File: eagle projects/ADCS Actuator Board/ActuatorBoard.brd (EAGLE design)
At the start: 91 x 91 mm, 230 parts, among them J11 TE_1-84953-1, J2 TE_1-84953-1, J4 TE_1-84953-1, U10 LM2917MX/NOPB, U11 BD6210F-E2, U12 TSV991AILT, U13 LM2917MX/NOPB, U14 ADS7841E_2K5, U16 DRV10970_MOTOR_DRIVERDRV10970, U17 LM2917MX/NOPB, U18 BD6210F-E2, U19 TSV991AILT, U20 ADS7841E_2K5, U5 BD6210F-E2, U6 DRV10970_MOTOR_DRIVERDRV10970, U7 DRV10970_MOTOR_DRIVERDRV10970, U8 TSV991AILT, U9 ADS7841E_2K5

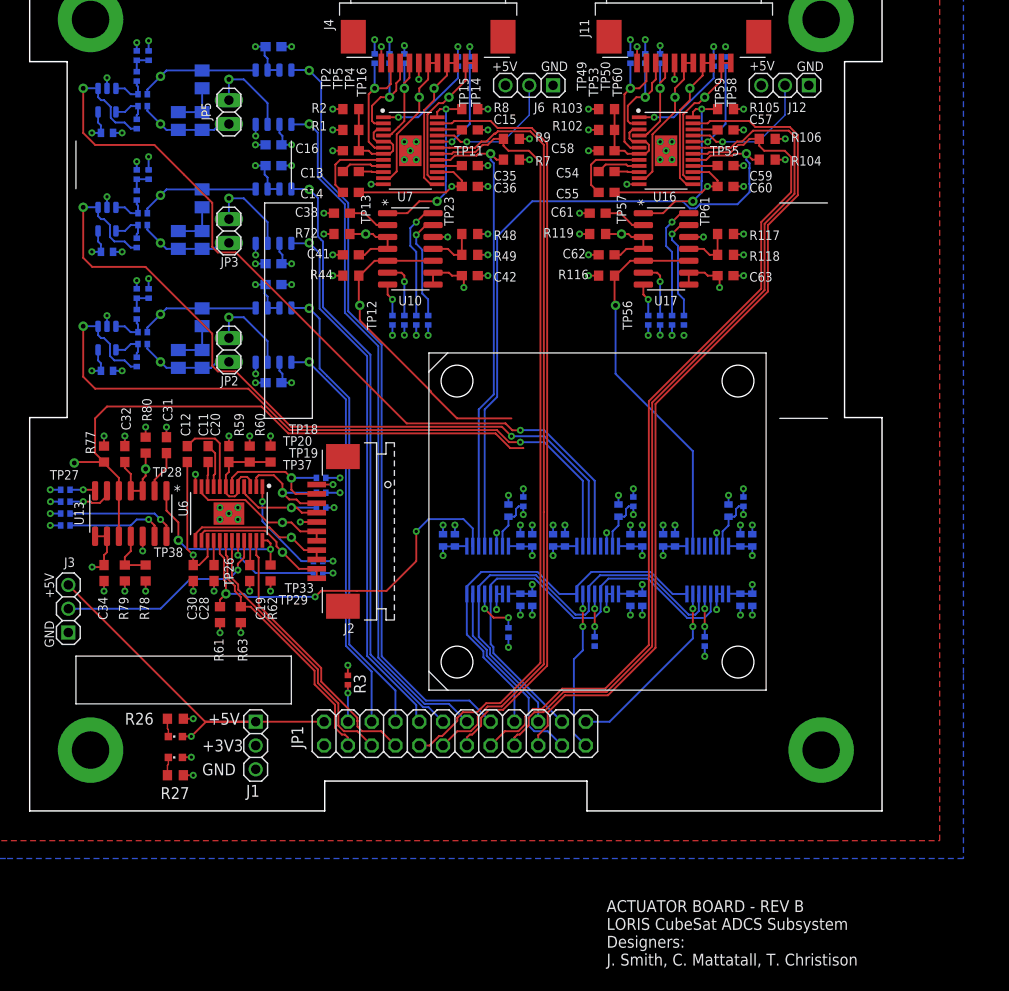
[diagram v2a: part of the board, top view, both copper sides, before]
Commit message: Added power connector and mobo-act brd mounting holes
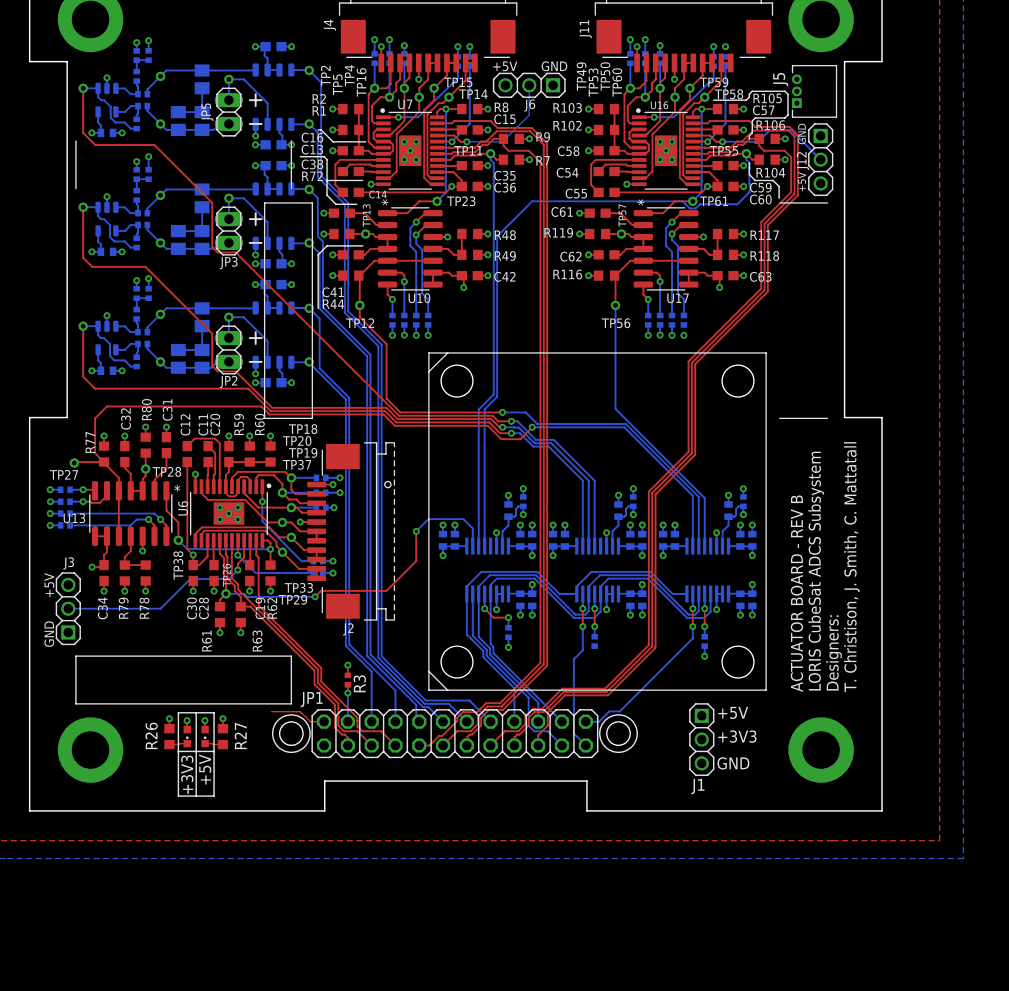
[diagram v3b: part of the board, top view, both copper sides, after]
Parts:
- added J5: TE-1734829-3, my_library:TE-1734829-3
- moved J1 47.6 mm to (71.8, 7.62)
- moved J12 8.80 mm to (84.5, 69.5), turned to 270 degrees
- moved R27 6.55 mm to (20.6, 7.94), turned to 270 degrees
- moved LED2 3.88 mm to (18.7, 7.94), turned to 180 degrees
- moved R26 2.01 mm to (14.9, 7.94), turned to 270 degrees
- moved LED1 1.27 mm to (16.8, 7.94), turned to 180 degrees
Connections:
- net +3V3: now also J5.2
- net +5V: now also J5.1
- net GND: now also J5.3
- net RW_Y_SPD: now also U20.4; no longer U20.2
- net RW_Z_SPD: now also U20.2; no longer U20.4
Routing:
- net +5V: track 146.0 -> 111.2 mm
- net RW_X_SPD: track 34.0 -> 65.9 mm, vias 0 -> 1
- net RW_Z_SPD: track 64.9 -> 91.6 mm, vias 0 -> 1
- net BRKMOD_Y: track 14.5 -> 15.8 mm
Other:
- board text added: "T. Christison, J. Smith, C. Mattatall"
- board text added: "TOP SIDE VIAS COVERED WITH SOLDERMASK"
- board text removed: "J. Smith, C. Mattatall, T. Christison"

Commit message: Rev B almost ready
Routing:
- net N$2: track 6.72 -> 0.00 mm, vias 1 -> 0
- net N$7: track 6.72 -> 0.00 mm, vias 1 -> 0
- net N$4: track 6.72 -> 0.00 mm, vias 1 -> 0
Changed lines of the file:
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@@
 <wire x1="24.13" y1="76.5175" x2="24.13" y2="75.2475" width="0.2032" layer="25"/>
 <wire x1="23.495" y1="73.3425" x2="24.765" y2="73.3425" width="0.2032" layer="25"/>
-<text x="0.635" y="96.52" size="1.778" layer="48">TOP SIDE VIAS COVERED WITH SOLDERMASK</text>
+<text x="0" y="93.345" size="1.778" layer="48">TOP SIDE VIAS COVERED WITH SOLDERMASK</text>
 <hole x="62.865" y="8.255" drill="2.5"/>
 <hole x="27.94" y="8.255" drill="2.5"/>
@@
 <wire x1="18.415" y1="74.61" x2="18.415" y2="77.155" width="0.2032" layer="16"/>
 </signal>
-<signal name="N$18">
-<wire x1="62.865" y1="31.4175" x2="62.865" y2="30.48" width="0.2032" layer="16"/>
-<wire x1="62.23" y1="29.845" x2="62.23" y2="28.2702" width="0.2032" layer="16"/>
-<wire x1="62.865" y1="30.48" x2="62.23" y2="29.845" width="0.2032" layer="16"/>
-<contactref element="C69" pad="1"/>
-<contactref element="R5" pad="1"/>
-<wire x1="64.4525" y1="32.52" x2="64.4525" y2="31.6394" width="0.2032" layer="16"/>
-<via x="64.4525" y="31.6394" extent="1-16" drill="0.35"/>
-<wire x1="63.66625" y1="31.58375" x2="63.5" y2="31.4175" width="0.2032" layer="16"/>
-<wire x1="63.5" y1="31.4175" x2="62.865" y2="31.4175" width="0.2032" layer="16"/>
-<contactref element="U9" pad="7"/>
-<wire x1="64.4525" y1="32.52" x2="63.9525" y2="32.52" width="0.2032" layer="16"/>
-<wire x1="63.66625" y1="32.23375" x2="63.66625" y2="31.58375" width="0.2032" layer="16"/>
-<wire x1="63.9525" y1="32.52" x2="63.66625" y2="32.23375" width="0.2032" layer="16"/>
-</signal>
 <signal name="N$25">
 <contactref element="U9" pad="13"/>
@@
 <contactref element="U9" pad="5"/>
 </signal>
-<signal name="N$33">
-<wire x1="51.1175" y1="31.4175" x2="51.1175" y2="30.48" width="0.2032" layer="16"/>
-<wire x1="50.4825" y1="29.845" x2="50.4825" y2="28.2702" width="0.2032" layer="16"/>
-<wire x1="51.1175" y1="30.48" x2="50.4825" y2="29.845" width="0.2032" layer="16"/>
-<contactref element="C76" pad="1"/>
-<contactref element="R29" pad="1"/>
-<wire x1="52.705" y1="32.52" x2="52.705" y2="31.6394" width="0.2032" layer="16"/>
-<via x="52.705" y="31.6394" extent="1-16" drill="0.35"/>
-<wire x1="51.91875" y1="31.58375" x2="51.7525" y2="31.4175" width="0.2032" layer="16"/>
-<wire x1="51.7525" y1="31.4175" x2="51.1175" y2="31.4175" width="0.2032" layer="16"/>
-<contactref element="U14" pad="7"/>
-<wire x1="52.705" y1="32.52" x2="52.205" y2="32.52" width="0.2032" layer="16"/>
-<wire x1="51.91875" y1="32.23375" x2="51.91875" y2="31.58375" width="0.2032" layer="16"/>
-<wire x1="52.205" y1="32.52" x2="51.91875" y2="32.23375" width="0.2032" layer="16"/>
-</signal>
 <signal name="N$45">
 <contactref element="U14" pad="13"/>
@@
 <contactref element="U14" pad="5"/>
 </signal>
-<signal name="N$58">
-<wire x1="74.6125" y1="31.4175" x2="74.6125" y2="30.48" width="0.2032" layer="16"/>
-<wire x1="73.9775" y1="29.845" x2="73.9775" y2="28.2702" width="0.2032" layer="16"/>
-<wire x1="74.6125" y1="30.48" x2="73.9775" y2="29.845" width="0.2032" layer="16"/>
-<contactref element="C90" pad="1"/>
-<contactref element="R50" pad="1"/>
-<wire x1="76.2" y1="32.52" x2="76.2" y2="31.6394" width="0.2032" layer="16"/>
-<via x="76.2" y="31.6394" extent="1-16" drill="0.35"/>
-<wire x1="75.41375" y1="31.58375" x2="75.2475" y2="31.4175" width="0.2032" layer="16"/>
-<wire x1="75.2475" y1="31.4175" x2="74.6125" y2="31.4175" width="0.2032" layer="16"/>
-<contactref element="U20" pad="7"/>
-<wire x1="76.2" y1="32.52" x2="75.7" y2="32.52" width="0.2032" layer="16"/>
-<wire x1="75.41375" y1="32.23375" x2="75.41375" y2="31.58375" width="0.2032" layer="16"/>
-<wire x1="75.7" y1="32.52" x2="75.41375" y2="32.23375" width="0.2032" layer="16"/>
-</signal>
 <signal name="N$59">
 <contactref element="U20" pad="13"/>
@@
 <wire x1="33.9725" y1="12.5894" x2="33.9725" y2="9.525" width="0.2032" layer="16"/>
 </signal>
+<signal name="N$2">
+<contactref element="U9" pad="7"/>
+<contactref element="R5" pad="1"/>
+<contactref element="C69" pad="1"/>
+<wire x1="62.865" y1="31.4175" x2="64.4525" y2="32.52" width="0" layer="19" extent="16-16"/>
+<wire x1="62.23" y1="28.2702" x2="62.865" y2="31.4175" width="0" layer="19" extent="16-16"/>
+</signal>
+<signal name="N$4">
+<contactref element="U14" pad="7"/>
+<contactref element="R29" pad="1"/>
+<contactref element="C76" pad="1"/>
+<wire x1="51.1175" y1="31.4175" x2="52.705" y2="32.52" width="0" layer="19" extent="16-16"/>
+<wire x1="50.4825" y1="28.2702" x2="51.1175" y2="31.4175" width="0" layer="19" extent="16-16"/>
+</signal>
+<signal name="N$7">
+<contactref element="U20" pad="7"/>
+<contactref element="R50" pad="1"/>
+<contactref element="C90" pad="1"/>
+<wire x1="74.6125" y1="31.4175" x2="76.2" y2="32.52" width="0" layer="19" extent="16-16"/>
+<wire x1="73.9775" y1="28.2702" x2="74.6125" y2="31.4175" width="0" layer="19" extent="16-16"/>
+</signal>
 </signals>

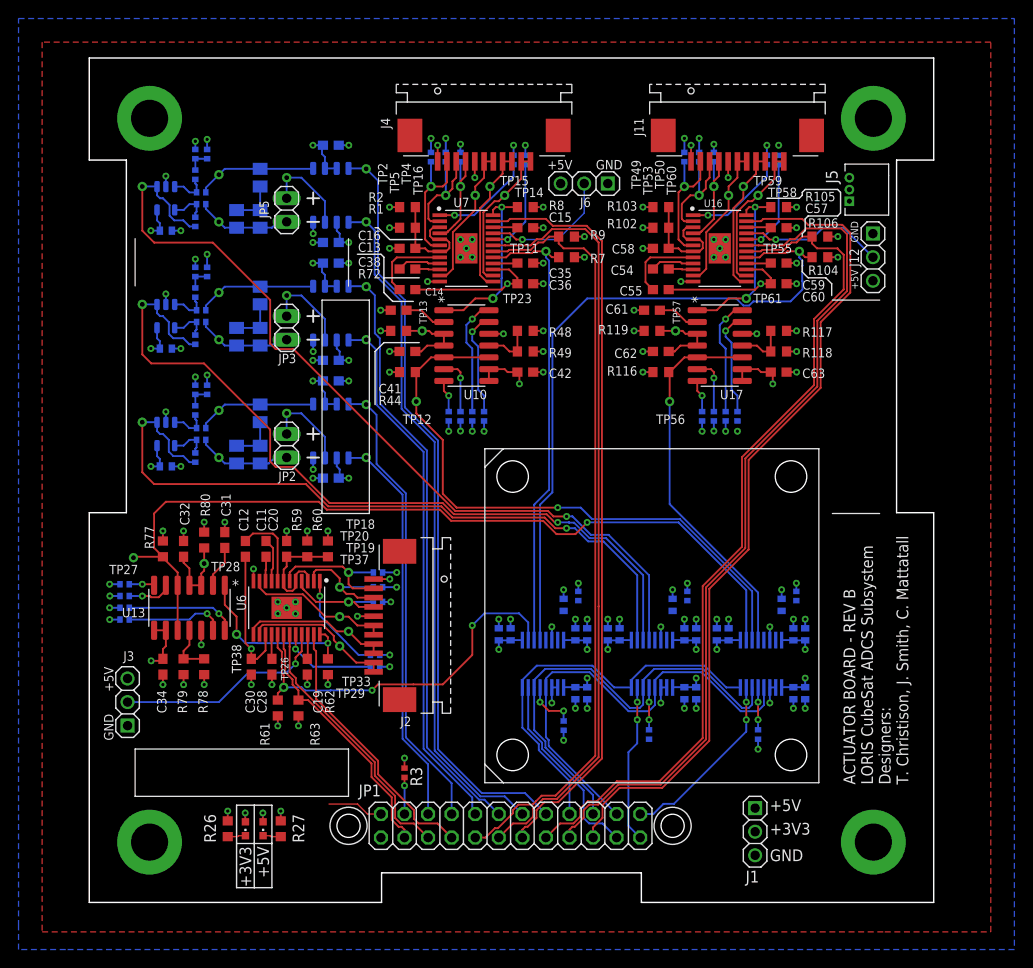
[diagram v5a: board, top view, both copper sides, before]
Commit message: Stitching vias, new current limit res for motors, updated motor retry cap
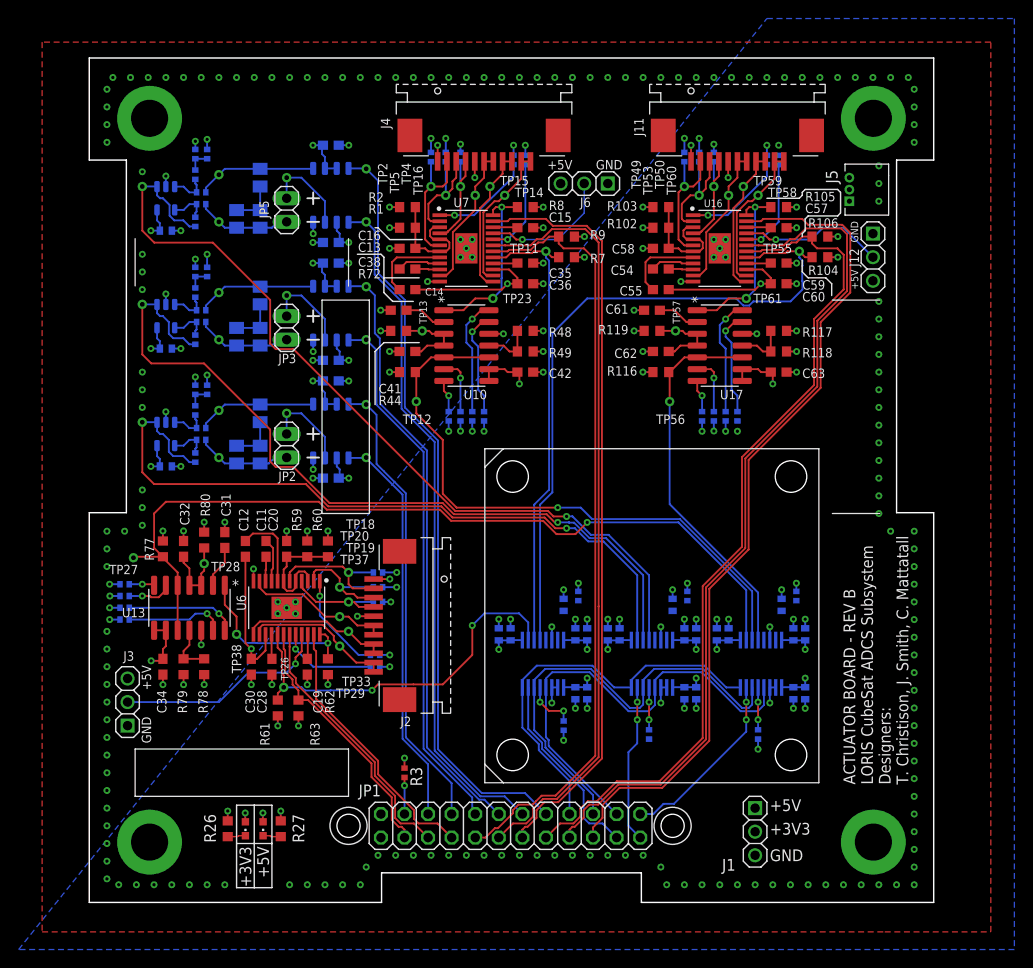
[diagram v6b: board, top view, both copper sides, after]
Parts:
- C15, C19, C57: value 0.33u -> 0.033u
- R104, R61, R7: value 75K -> 27K
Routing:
- net +5V: track 111.2 -> 105.2 mm
- net GND: vias 128 -> 293

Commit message: Replaced h-bridges with substitute part
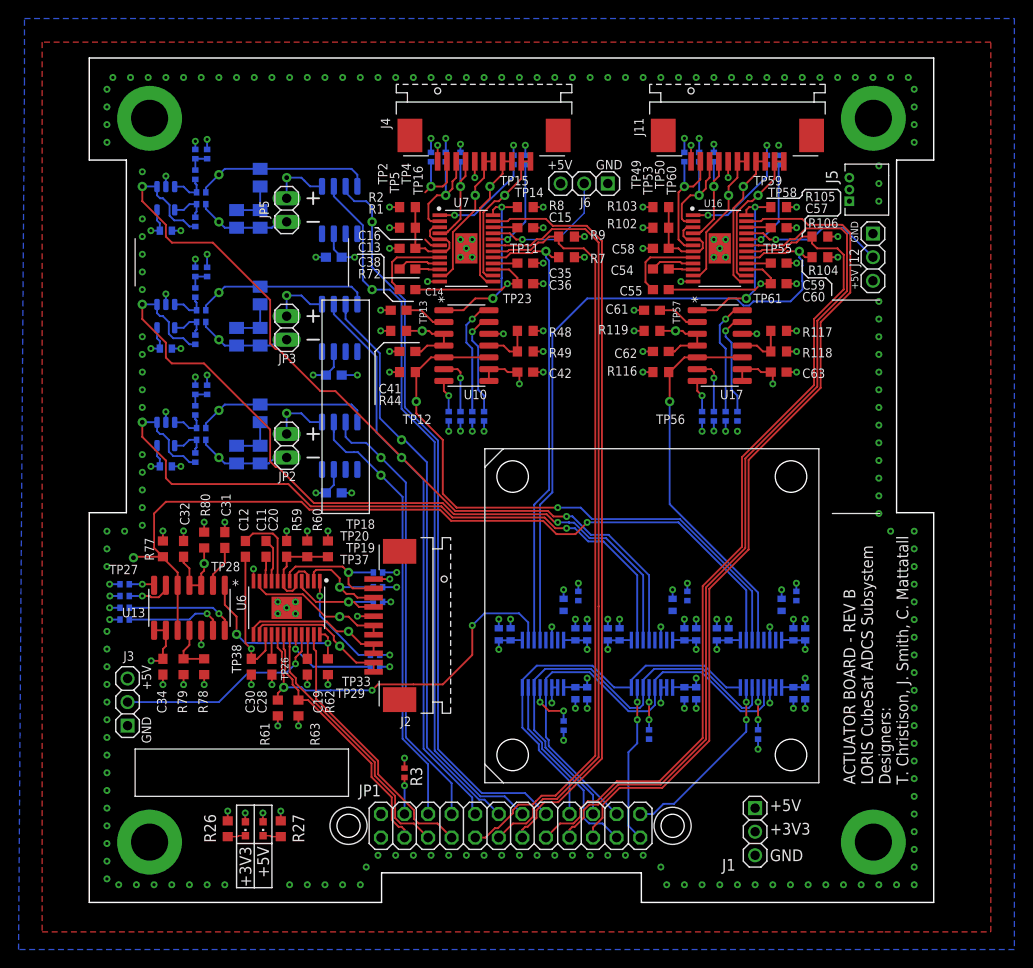
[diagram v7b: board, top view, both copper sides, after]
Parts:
- removed C27, C45, C50, C51: 0.1u, rcl:C0603
- removed U11, U18, U5: BD6210F-E2, my_library:BD6221F-E2_SOIC8P127_500X620X171L30X42N
- added C4: 0.1u, rcl:C0603
- added U1, U2, U3: SIP2100DY-T1-GE3, my_library:SOIC8P127_490X600X175L71X43N_SIP2100DY-T1-GE3
- C31, C38, C61: value 0.01u -> 0.056u
- moved TP24 16.9 mm to (33.7, 49.8)
- moved TP25 13.3 mm to (33.7, 47.9)
- moved TP48 7.33 mm to (30.5, 66.0)
- moved TP8 5.93 mm to (31.4, 47.9)
- moved TP47 5.75 mm to (30.5, 73.3)
- moved TP9 2.48 mm to (31.4, 46.0)
- moved C1 1.62 mm to (26.4, 44.1), turned to 180 degrees
- moved C2 0.71 mm to (26.4, 56.8)
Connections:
- net +5V: now also C4.2, U1.3, U2.3, U3.3; no longer C27.1, C45.2, C50.1, C51.2, U11.2, U11.3, U11.6, U18.2, U18.3, U18.6, U5.2, U5.3, U5.6
- net GND: now also C4.1, U1.1, U1.2, U1.4, U2.1, U2.2, U2.4, U3.1, U3.2, U3.4; no longer C27.2, C45.1, C50.2, C51.1, U11.8, U18.8, U5.8
- net MAG_CUR_SEN_X: now also U1.8; no longer U5.1
- net MAG_CUR_SEN_Y: now also U2.8; no longer U11.1
- net MAG_CUR_SEN_Z: now also U3.8; no longer U18.1
- net MAG_X_FIN: now also U1.7; no longer U5.4
- net MAG_X_RIN: now also U1.6; no longer U5.5
- net MAG_Y_FIN: now also U2.7; no longer U11.4
- net MAG_Y_RIN: now also U2.6; no longer U11.5
- net MAG_Z_FIN: now also U3.7; no longer U18.4
- net MAG_Z_RIN: now also U3.6; no longer U18.5
- net OUT2_X: now also U1.5; no longer U5.7
- net OUT2_Y: now also U2.5; no longer U11.7
- net OUT2_Z: now also U3.5; no longer U18.7
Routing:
- net +5V: track 105.2 -> 93.0 mm, vias 31 -> 28
- net GND: track 126.7 -> 120.4 mm
- net MAG_CUR_SEN_Z: track 12.9 -> 19.2 mm
- net MAG_CUR_SEN_X: track 12.9 -> 19.2 mm
- net MAG_CUR_SEN_Y: track 12.9 -> 19.2 mm
- net MAG_X_RIN: track 43.1 -> 48.3 mm
- net X_HALL_C: track 14.6 -> 9.57 mm
- net MAG_Z_RIN: track 74.2 -> 78.8 mm
- net MAG_Y_RIN: track 57.9 -> 61.3 mm
- net OUT2_Z: track 9.67 -> 6.42 mm
- net OUT2_X: track 9.67 -> 6.42 mm
- net OUT2_Y: track 9.80 -> 6.55 mm
- net MAG_Z_FIN: track 82.2 -> 80.1 mm
- net MAG_Y_FIN: track 65.0 -> 63.4 mm
- net MAG_X_FIN: track 49.9 -> 48.6 mm
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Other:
- board text removed: "TOP SIDE VIAS COVERED WITH SOLDERMASK"
